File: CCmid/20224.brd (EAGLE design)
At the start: 33.7 x 20.3 mm, 17 parts, among them J3 9296006, K1 PC357NJ0000F, U1 AL8862

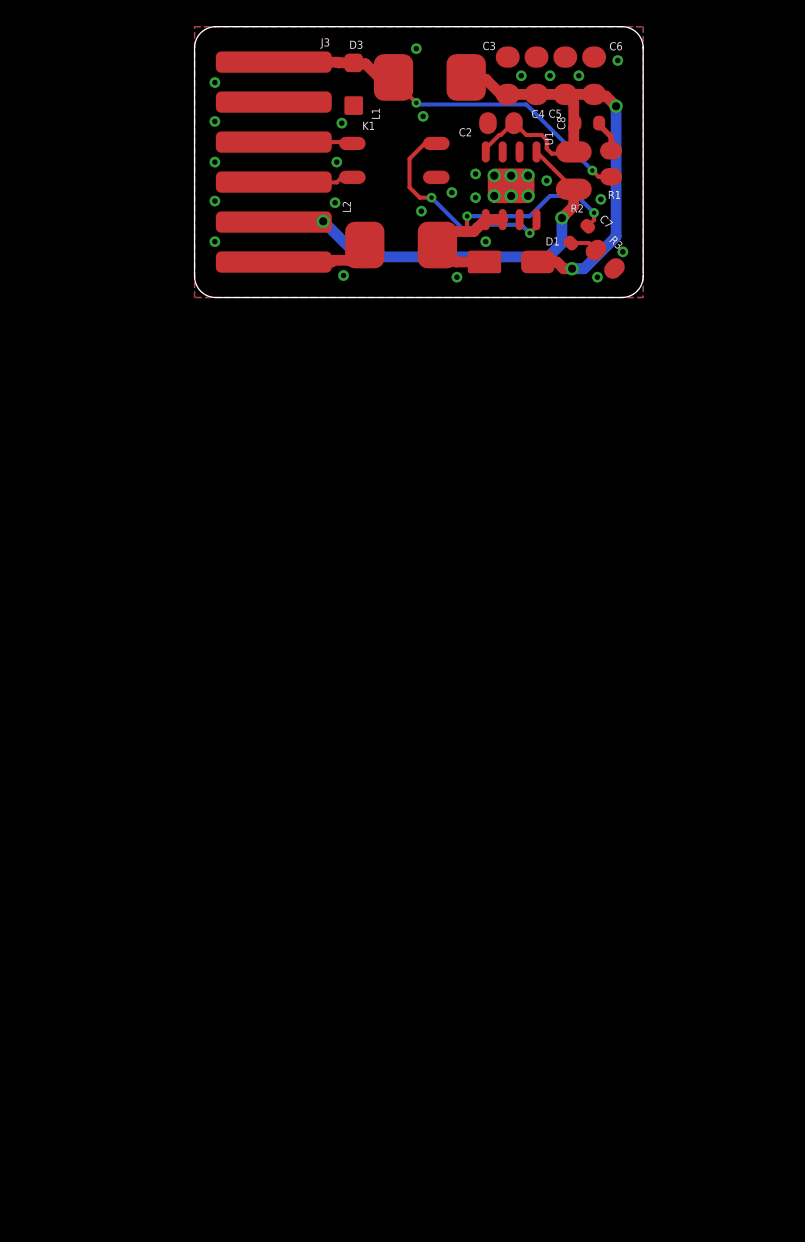
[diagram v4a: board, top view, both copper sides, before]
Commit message: CCmid: fix inrush on schm
inrush 3A6 with 36V step
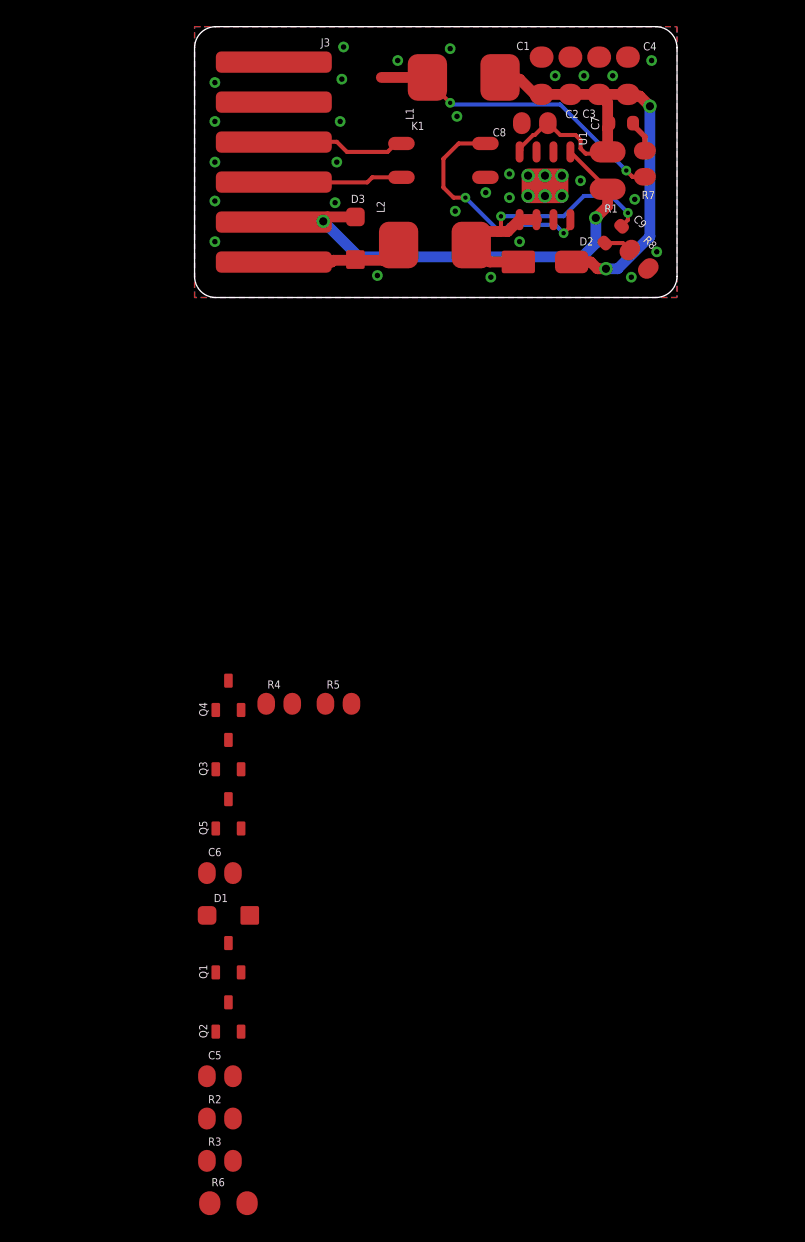
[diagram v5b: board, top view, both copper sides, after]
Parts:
- added C1: 10uF, C-C:C1206(3216)
- added C9: 470pF, C-C:C0603(1608)
- added D2: SQ4, D-SBR:SMA
- added Q1, Q2, Q4: K1N, Q-NPN:SOT23
- added Q3, Q5: P65, Q-PCH:SOT23
- added R4: DNP, R-C:C0805(2012)
- added R5: 49.9k, R-C:C0805(2012)
- added R6: 10, R-C:C1206(3216)
- added R7: 482, R-C:C0805(2012)
- added R8: 3.3, R-C:C0805(2012)
- C2: value .1uF -> 10uF; device C-C:C0805(2012) -> C-C:C1206(3216)
- C5: value 10uF -> .1uF; device C-C:C1206(3216) -> C-C:C0805(2012)
- C6: value 10uF -> 1uF; device C-C:C1206(3216) -> C-C:C0805(2012)
- C7: value 470pF -> 680pF
- C8: value 680pF -> .1uF; device C-C:C0603(1608) -> C-C:C0805(2012)
- D1: value SQ4 -> SMF36CA; device D-SBR:SMA -> D-TVS:SOD123
- R1: value 482 -> 0.15; device R-C:C0805(2012) -> R-C:C1210(3225)
- R2: value 0.15 -> 100k; device R-C:C1210(3225) -> R-C:C0805(2012)
- R3: value 3.3 -> 49.9
- moved C5 79.4 mm to (1.91, -58.4), turned to 0 degrees
- moved R2 75.9 mm to (1.91, -61.6), turned to 0 degrees
- moved R3 73.6 mm to (1.91, -64.8), turned to 0 degrees
- moved C6 66.1 mm to (1.91, -43.2), turned to 0 degrees
- moved D1 53.4 mm to (2.54, -46.4), turned to 0 degrees
- moved D3 11.6 mm to (12.1, 4.45)
- moved C7 8.94 mm to (32.0, 13.1), turned to 0 degrees
- moved C3 6.86 mm to (30.4, 16.6)
- moved C4 6.86 mm to (32.5, 16.6)
- moved C2 6.31 mm to (28.2, 16.6), turned to 90 degrees
- moved C8 3.94 mm to (25.5, 13.1), turned to 180 degrees
- moved K1 3.68 mm to (18.7, 10.3)
- moved L1 2.54 mm to (20.2, 16.5)
- moved U1 2.54 mm to (26.3, 8.38)
- moved L2 2.54 mm to (18.0, 3.94)
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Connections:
- new net N$10: Q2.E, R3.1
- new net N$32: C6.1, Q2.C, Q3.2(S), Q4.E, Q5.2(S), R4.2, R6.1
- new net N$33: C6.2, Q3.1(G), Q4.B, Q4.C, Q5.1(G), R3.2, R4.1, R5.2
- new net N$8: D1.C, J3.1, Q1.B, Q3.3(D)
- new net N$9: C5.1, Q1.C, Q2.B, R2.2
- net +CH: now also D3.C, R1.1; no longer R2.1
- net -CH: now also D3.A
- net 0V: now also C1.2, C8.2, D1.A, R2.1, R5.1, R8.1; no longer C6.2, D3.A, R3.1
- net BULK: now also C1.1, C7.1, D2.K, R1.2; no longer C5.1, C6.1, D1.K, R2.2
- net N$3: now also C9.1, D2.A; no longer C7.1, D1.A
- net N$5: now also Q5.3(D), R6.2, R7.1; no longer D3.C, J3.1, R1.1
- net N$6: now also C9.2, R8.2; no longer C7.2, R3.2
- net N$7: now also C7.2, R7.2; no longer C8.2, R1.2
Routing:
- net N$5: track 29.1 -> 23.0 mm
- net +CH: track 31.6 -> 36.7 mm
- net N$2: track 5.93 -> 10.2 mm
- net N$4: track 6.06 -> 9.74 mm
- net -CH: track 7.35 -> 10.0 mm
- net N$1: track 16.5 -> 17.7 mm
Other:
- board size 33.7 x 20.3 mm -> 36.2 x 20.3 mm

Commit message: CCmid: bom, surge sim
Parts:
- removed R8: 3.3, R-C:C0805(2012)
- added TP1: TPPAD1-06, J-TP:P1-06
- R1: value 0.15 -> 100k; device R-C:C1210(3225) -> R-C:C0805(2012)
- R2: value 100k -> 49.9
- R3: value 49.9 -> 49.9k
- R4: value DNP -> 10; device R-C:C0805(2012) -> R-C:C1206(3216)
- R5: value 49.9k -> 499
- R6: value 10 -> 3.3; device R-C:C1206(3216) -> R-C:C0805(2012)
- R7: value 482 -> 0.15; device R-C:C0805(2012) -> R-C:C1210(3225)
- moved R6 80.6 mm to (41.0, 2.87), turned to 135 degrees
- moved R3 74.9 mm to (18.2, 8.38), turned to 90 degrees
- moved R2 72.5 mm to (16.4, 9.40), turned to 270 degrees
- moved C5 68.2 mm to (14.5, 8.64), turned to 270 degrees
- moved Q2 67.7 mm to (13.5, 12.8)
- moved Q1 66.4 mm to (14.6, 15.7), turned to 180 degrees
- moved D1 63.1 mm to (11.7, 16.1), turned to 270 degrees
- moved Q5 58.4 mm to (21.6, 16.5), turned to 270 degrees
- moved C6 56.4 mm to (20.3, 10.2), turned to 270 degrees
- moved Q3 53.4 mm to (18.0, 16.8)
- moved R5 50.8 mm to (41.4, 10.0), turned to 90 degrees
- moved R4 46.8 mm to (21.5, 13.8)
- moved Q4 45.5 mm to (17.5, 13.1)
- moved R1 18.6 mm to (12.4, 8.64)
- moved C8 8.13 mm to (33.7, 13.3)
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- renumbered J3 to J1
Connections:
- net +CH: now also R7.1; no longer R1.1
- net 0V: now also R1.1, R3.1, R6.1; no longer R2.1, R5.1, R8.1
- net BULK: now also R7.2; no longer R1.2
- net N$10: now also R2.1; no longer R3.1
- net N$3: now also TP1.TP
- net N$32: now also R4.1; no longer R4.2, R6.1
- net N$33: now also R2.2; no longer R4.1, R5.2
- net N$5: now also R4.2, R5.1; no longer R6.2, R7.1
- net N$6: now also R6.2; no longer R8.2
- net N$7: now also R5.2; no longer R7.2
- net N$9: now also R1.2; no longer R2.2
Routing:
- net N$33: track 0.00 -> 20.2 mm, vias 0 -> 2
- net N$32: track 0.00 -> 16.3 mm, vias 0 -> 2
- net +CH: track 36.7 -> 52.9 mm
- net N$8: track 0.00 -> 13.8 mm
- net N$2: track 10.2 -> 23.7 mm, vias 0 -> 2
- net N$4: track 9.74 -> 20.9 mm, vias 0 -> 2
- net N$9: track 0.00 -> 8.17 mm
- net -CH: track 10.0 -> 17.9 mm
- net N$10: track 0.00 -> 2.53 mm
- net N$5: track 23.0 -> 25.5 mm
- net N$1: track 17.7 -> 18.4 mm
- net N$3: track 22.8 -> 23.1 mm, vias 2 -> 1
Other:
- board size 36.2 x 20.3 mm -> 43.8 x 20.3 mm
- board text added: "+CH"
- board text added: "-CH"
- board text added: "A"
- board text added: "GND"
- board text added: "K"
- board text added: "VIN"
